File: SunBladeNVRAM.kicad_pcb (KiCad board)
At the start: 2 copper layers, 36.5 x 18.5 mm, 10 parts, among them J1 Conn_01x14_Pin, J2 Conn_01x14_Pin, J3 Conn_01x02_Pin, J4 Conn_01x02_Pin, J5 Conn_01x01_Pin, J6 Conn_01x01_Pin, J7 Conn_01x01_Pin, J8 Conn_01x01_Pin, U1 M48T59Y-70MH1, Y1 32.768 kHz

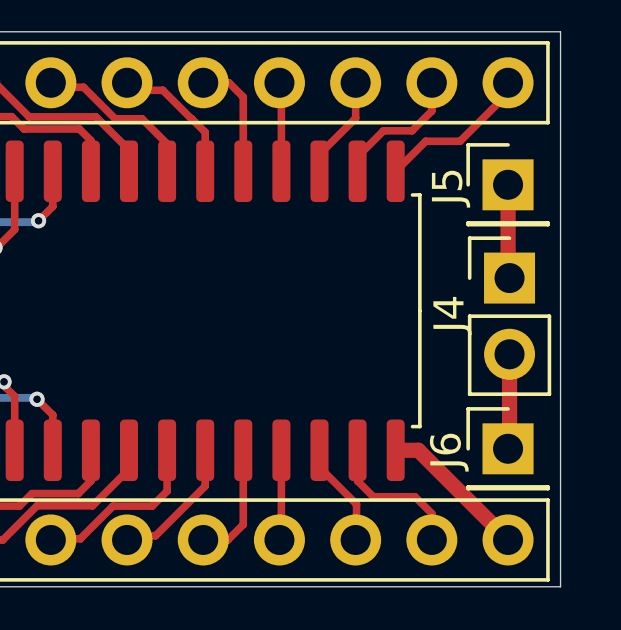
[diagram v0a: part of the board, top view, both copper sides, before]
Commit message: mark +/- pins for battery connection to M48T59Y
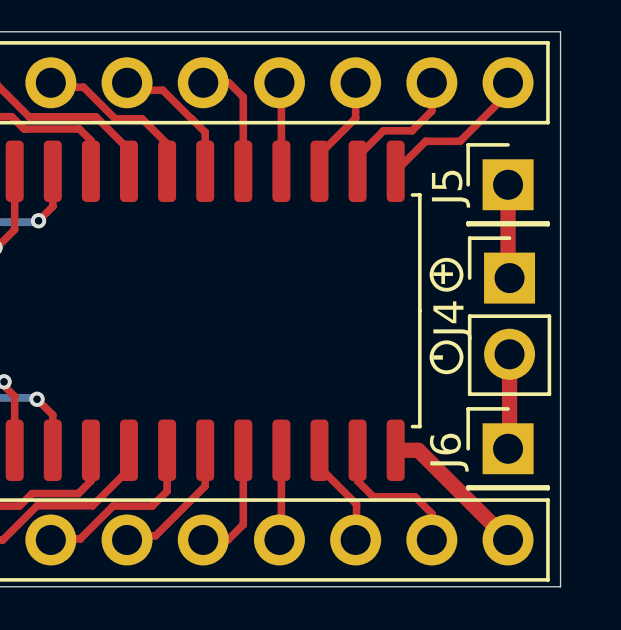
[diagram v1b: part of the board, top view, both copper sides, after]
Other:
- board text added: "+"
- board text added: "-"
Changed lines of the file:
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@@
 		(tags "Through hole pin header THT 1x02 2.54mm single row")
 		(property "Reference" "J4"
-			(at -2 1.19 90)
+			(at -2 1.34 90)
 			(layer "F.SilkS")
 			(effects
@@
 			)
 		)
+	)
+	(gr_circle
+		(center 115.95 77.9)
+		(end 116.35 78.2)
+		(stroke
+			(width 0.127)
+			(type default)
+		)
+		(fill none)
+		(layer "F.SilkS")
+	)
+	(gr_circle
+		(center 115.95 80.65)
+		(end 116.35 80.95)
+		(stroke
+			(width 0.127)
+			(type default)
+		)
+		(fill none)
+		(layer "F.SilkS")
 	)
 	(gr_rect
@@
 		)
 	)
+	(gr_text "-"
+		(at 115.45 81.05 0)
+		(layer "F.SilkS")
+		(effects
+			(font
+				(size 0.762 0.762)
+				(thickness 0.127)
+				(bold yes)
+			)
+			(justify left bottom)
+		)
+	)
+	(gr_text "+"
+		(at 115.4 78.3 0)
+		(layer "F.SilkS")
+		(effects
+			(font
+				(size 0.762 0.762)
+				(thickness 0.127)
+				(bold yes)
+			)
+			(justify left bottom)
+		)
+	)

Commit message: improved 1x14 header, M48T59Y-MH footprints
The 1x14 header footprint is for round (machine pin)
headers, which is what we want to use. The through holes
are much more compact than the footprint for normal
square headers.

The M48T59Y footprint is made slightly more compact.
It should still allow plenty of room to solder on the
M49T59Y, but it fits relatively comfortably between
the 1x14 pin headers.

With these changes, it shouldn't be necessary to bend
the legs of the M48T59Y.
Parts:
- J1, J2: footprint Connector_PinHeader_2.54mm:PinHeader_1x14_P2.54mm_Vertical -> SunBladeNVRAM:SAMTEC_BBL-114-T-E
- U1: footprint Package_SO:SOIC-28W_7.5x17.9mm_P1.27mm -> SunBladeNVRAM:M48T59Y-MH
- moved J1 15.2 mm to (85.0, 71.5), turned to 0 degrees
- moved J2 15.2 mm to (85.0, 86.7), turned to 0 degrees
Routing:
- net Net-(J1-Pin_1): track 21.7 -> 0.00 mm
- net Net-(J2-Pin_2): track 19.5 -> 0.00 mm
- net Net-(J1-Pin_2): track 19.1 -> 0.00 mm, vias 2 -> 0
- net Net-(J2-Pin_3): track 17.6 -> 0.00 mm, vias 2 -> 0
- net Net-(J1-Pin_3): track 16.8 -> 0.00 mm, vias 2 -> 0
- net Net-(J2-Pin_4): track 14.9 -> 0.14 mm, vias 2 -> 0
- net Net-(J1-Pin_4): track 14.7 -> 0.00 mm, vias 2 -> 0
- net Net-(J2-Pin_1): track 14.7 -> 0.00 mm, vias 1 -> 0
- net Net-(J1-Pin_5): track 12.5 -> 0.00 mm, vias 2 -> 0
- net Net-(J2-Pin_5): track 12.4 -> 0.32 mm, vias 2 -> 0
- net Net-(J1-Pin_6): track 8.25 -> 0.00 mm
- net Net-(J2-Pin_6): track 8.24 -> 0.00 mm
- net Net-(J2-Pin_7): track 7.41 -> 0.00 mm
- net Net-(J1-Pin_7): track 6.76 -> 0.00 mm
- net Net-(J3-Pin_2): track 6.19 -> 0.00 mm
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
